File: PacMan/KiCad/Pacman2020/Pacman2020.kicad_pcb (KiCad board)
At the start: 2 copper layers, 109.2 x 73.7 mm, 50 parts, among them J1 DF22-1P-7.92DSA(05), J10 Conn_01x02, J11 Conn_01x02, J12 Conn_01x02, J13 Conn_01x08, J2 DF22-1P-7.92DSA(05), J3 DF22-1P-7.92DSA(05), J4 JST PH, J5 Conn_02x03_Odd_Even, J6 Conn_01x01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

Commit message: notes from design review 1
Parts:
- removed G***: LOGO, AERO_CUSTOM:pacman-logo-silkscreen
- removed J6, J7: Conn_01x01, Connector_Hirose:Hirose_DF63R-1P-3.96DSA_1x01_P3.96mm_Vertical
- moved R5 82.2 mm to (106.4, 140.8)
- moved J8 49.1 mm to (166.2, 144.5), turned to 270 degrees
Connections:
- J13 pad 4: +12V -> /CONTACTOR
- J13 pad 5: /PRECHARGE -> GND
- J13 pad 6: /CONTACTOR -> /SHUTDOWN_IN
- J13 pad 7: /SHUTDOWN_IN -> GND
- J13 pad 8: GND -> /PRECHARGE
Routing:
- net /SHUTDOWN_IN: track 18.2 -> 119.6 mm
- net /CONTACTOR: track 3.68 -> 58.3 mm
- net /PRECHARGE: track 2.07 -> 19.8 mm
- net GND: vias 7 -> 11

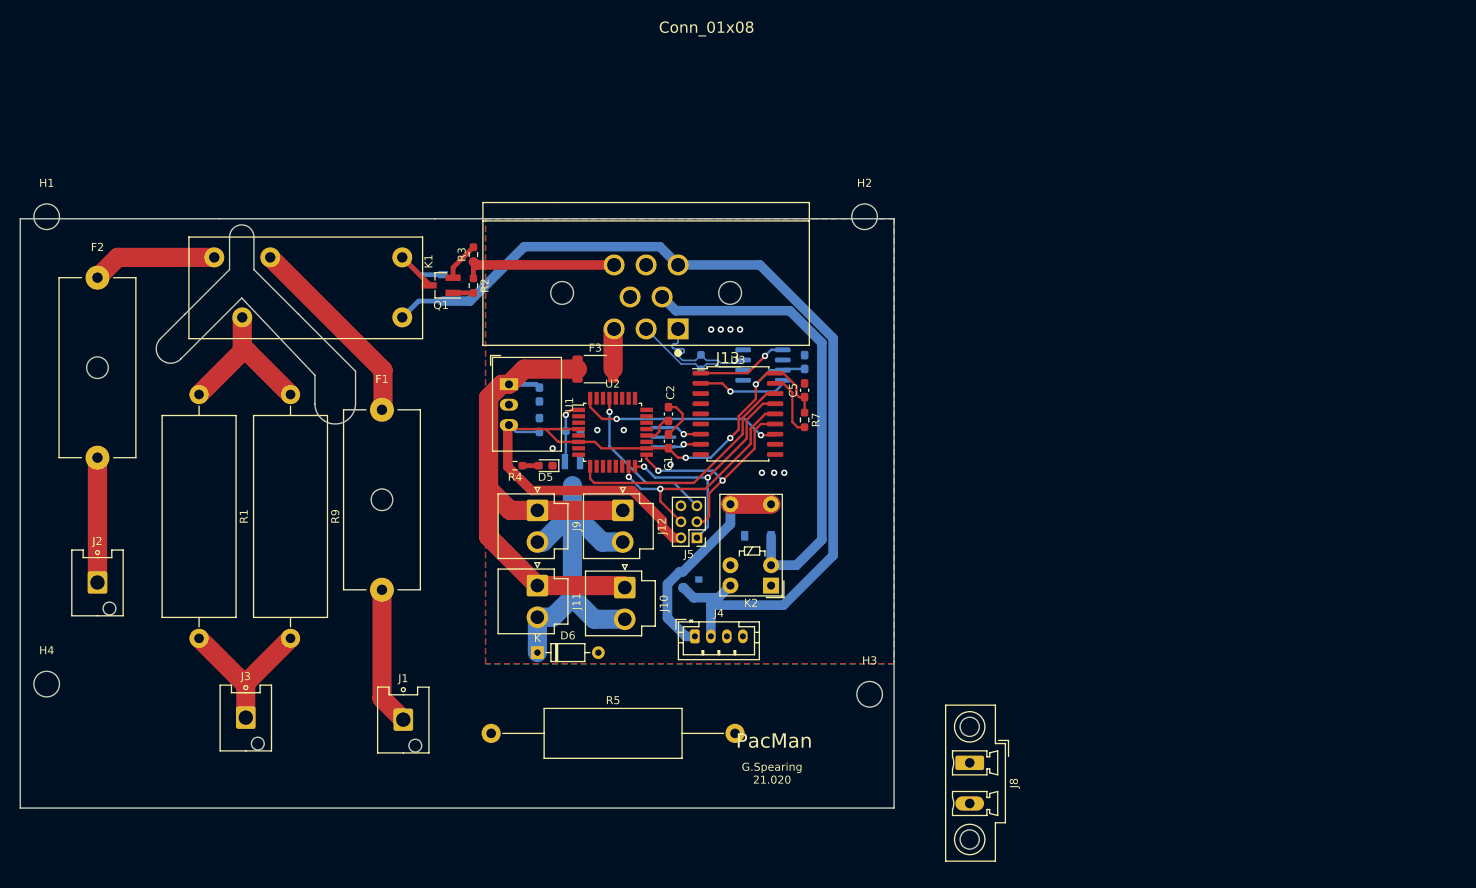
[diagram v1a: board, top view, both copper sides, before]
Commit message: remove ATMEGA, add BMS fan control
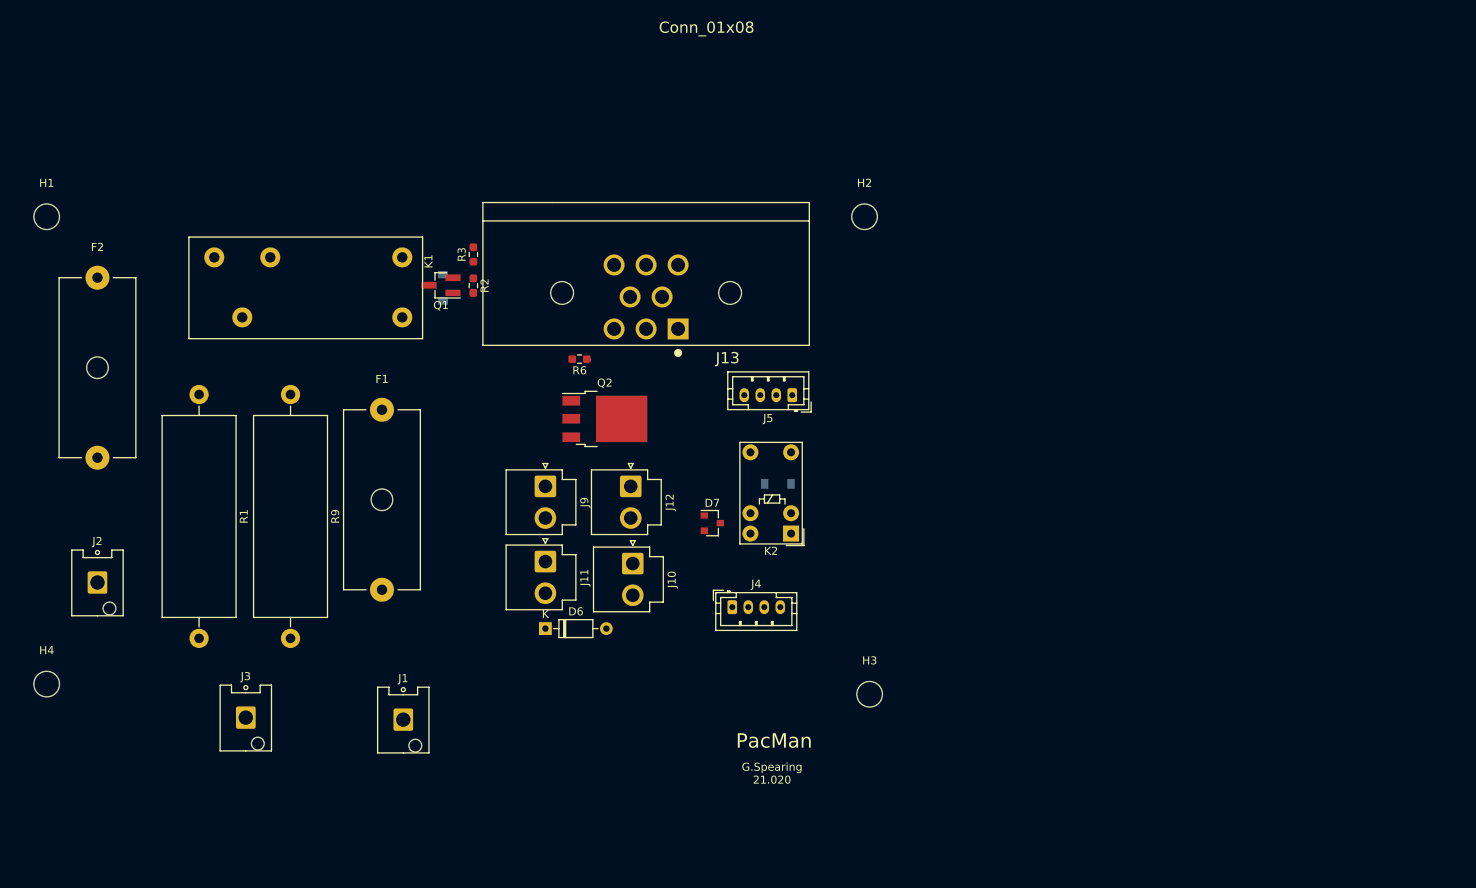
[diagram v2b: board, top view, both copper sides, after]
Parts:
- removed C1, C2, C5, C6: 0.1u, Capacitor_SMD:C_0603_1608Metric_Pad1.08x0.95mm_HandSolder
- removed C3: 1u, Capacitor_SMD:C_0603_1608Metric_Pad1.08x0.95mm_HandSolder
- removed C4: 10u, Capacitor_SMD:C_0603_1608Metric_Pad1.08x0.95mm_HandSolder
- removed D5: LED, LED_SMD:LED_0603_1608Metric_Pad1.05x0.95mm_HandSolder
- removed F3: MF-MSMF050, Fuse:Fuse_1812_4532Metric_Pad1.30x3.40mm_HandSolder
- removed J8: Conn_01x02, Connector_Phoenix_MC_HighVoltage:PhoenixContact_MCV_1,5_2-GF-5.08_1x02_P5.08mm_Vertical_ThreadedFlange_MountHole
- removed R4: 330, Resistor_SMD:R_0603_1608Metric_Pad0.98x0.95mm_HandSolder
- removed R5: 39k, Resistor_THT:R_Axial_DIN0617_L17.0mm_D6.0mm_P30.48mm_Horizontal
- removed R7: 10K, Resistor_SMD:R_0603_1608Metric_Pad0.98x0.95mm_HandSolder
- removed R8: 120, Resistor_SMD:R_0603_1608Metric_Pad0.98x0.95mm_HandSolder
- removed U1: R-785.0-1.0, Converter_DCDC:Converter_DCDC_RECOM_R-78E-0.5_THT
- removed U2: ATmega328P-AU, Package_QFP:TQFP-32_7x7mm_P0.8mm
- removed U3: MCP2515-xSO, Package_SO:SOIC-18W_7.5x11.6mm_P1.27mm
- removed U4: MCP2551-I-SN, Package_SO:SOIC-8_3.9x4.9mm_P1.27mm
- removed Y1: 16MHz, AERO_CUSTOM:Resonator_SMD_muRata_CSTxExxV-3Pin_3.0x1.1mm_HandSoldering
- D7, R6: moved to F.Cu
- J5: value Conn_02x03_Odd_Even -> Conn_01x04; footprint Connector_PinHeader_2.00mm:PinHeader_2x03_P2.00mm_Vertical -> Connector_JST:JST_PH_B4B-PH-K_1x04_P2.00mm_Vertical
- Q2: value DMN3404L -> Q_NMOS_GDS; footprint Package_TO_SOT_SMD:SOT-23_Handsoldering -> Package_TO_SOT_SMD:TO-252-3_TabPin2; moved to F.Cu
- moved J5 21.4 mm to (144.0, 98.5)
- moved R6 9.03 mm to (117.4, 94.0), turned to 180 degrees
- moved Q2 7.94 mm to (120.6, 101.5), turned to 0 degrees
- moved D7 7.53 mm to (134.0, 114.5)
- moved D2 6.96 mm to (142.2, 109.6)
- moved K2 6.96 mm to (143.9, 115.8)
- moved J4 5.93 mm to (136.5, 125.0)
- moved J10 3.16 mm to (124.1, 119.6)
- moved J11 3.16 mm to (113.1, 119.3)
- moved J12 3.16 mm to (123.8, 109.9)
- moved J9 3.16 mm to (113.1, 109.9)
- moved D6 3.16 mm to (113.1, 127.7)
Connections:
- net Net-(F1-Pad2) renamed /pre/discharge/INT-
- net Net-(F2-Pad2) renamed /pre/discharge/BATT+
- net Net-(J3-Pad1) renamed /pre/discharge/INT+
- D7 pad 1: /SHUTDOWN_IN -> /pre/discharge/AIR_B+
- D7 pad 2: /pre/discharge/AIR_B+ -> /SHUTDOWN_IN
- J13 pad 3: +12V -> /FAN_CTRL
- J13 pad 5: GND -> +12V
- J5 pad 1: /MISO -> /CAN+
- J5 pad 2: +5V -> /CAN-
- J5 pad 3: /SCK -> +12V
- J5 pad 4: /MOSI -> GND
- K2 pad 1: (no net) -> Net-(K2-Pad1)
- Q1 pad 2: Net-(Q1-Pad2) -> GND
- Q2 pad 2: GND -> /FAN_OUT
- Q2 pad 3: /FAN_OUT -> GND
- R3 pad 2: Net-(Q1-Pad2) -> GND
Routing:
- net /SHUTDOWN_IN: track 119.6 -> 0.00 mm
- net +5V: track 95.2 -> 0.00 mm, vias 3 -> 0
- net /12_IN: track 71.5 -> 0.00 mm
- net /CONTACTOR: track 58.3 -> 0.00 mm
- net /FAN_OUT: track 45.2 -> 0.00 mm
- net /MISO: track 31.4 -> 0.00 mm, vias 2 -> 0
- net /CAN_CS: track 30.7 -> 0.00 mm
- net /MOSI: track 30.4 -> 0.00 mm, vias 2 -> 0
- net /SCK: track 29.0 -> 0.00 mm, vias 2 -> 0
- net /pre/discharge/AIR_B+: track 27.2 -> 0.00 mm
- net /CAN_INT: track 25.7 -> 0.00 mm, vias 2 -> 0
- net Net-(F1-Pad1): track 24.9 -> 0.00 mm
- net /pre/discharge/INT+: track 20.4 -> 0.00 mm
- net Net-(K1-Pad5): track 20.1 -> 0.00 mm
- net /RESET: track 20.0 -> 0.00 mm, vias 1 -> 0
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- removed copper zone on B.Cu, net GND
- removed copper zone on F.Cu, net GND
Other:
- board outline removed

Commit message: update schematic and layout
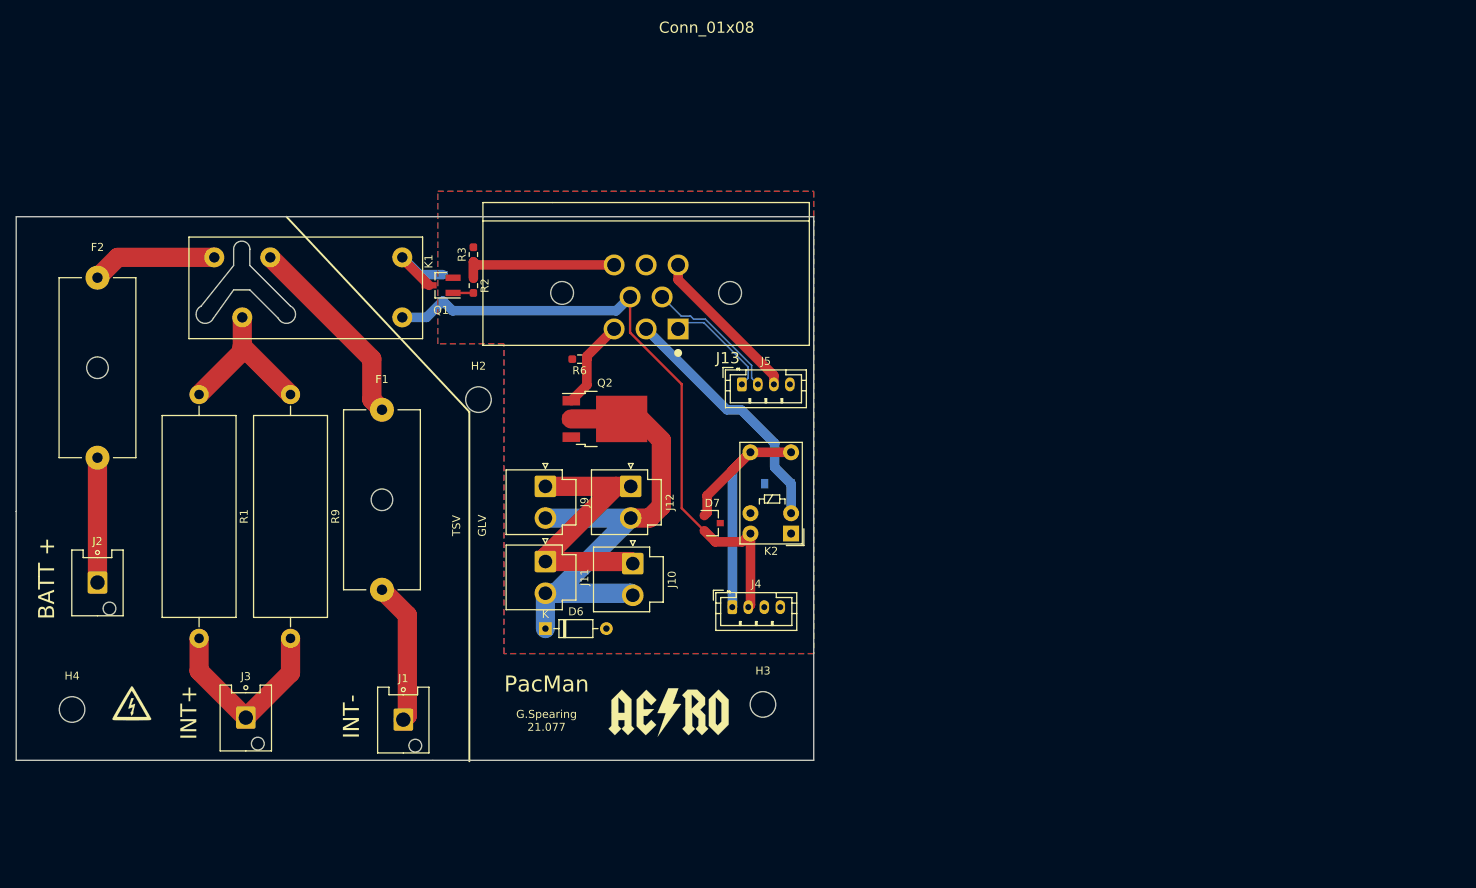
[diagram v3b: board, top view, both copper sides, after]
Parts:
- removed H1: MountingHole, MountingHole:MountingHole_3.2mm_M3
- added G***: LOGO, AERO_CUSTOM:AERO_Logo_15x6mm, F.Cu at (128.5, 138.2)
- added Ref**: Val**, AERO_Logo:hv_small, F.Cu at (61.5, 139.2)
- moved H2 53.4 mm to (104.8, 99.1)
- moved H3 13.4 mm to (140.3, 137.2)
- moved J5 6.44 mm to (137.7, 97.2), turned to 0 degrees
- moved H4 4.49 mm to (54.0, 137.8)
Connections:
- J13 pad 2: /CAN- -> /CONTACTOR
- J13 pad 4: /CONTACTOR -> /CAN-
- J13 pad 5: +12V -> /SHUTDOWN_IN
- J13 pad 6: /SHUTDOWN_IN -> +12V
- K2 pad 1: Net-(K2-Pad1) -> (no net)
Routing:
- net /SHUTDOWN_IN: track 0.00 -> 79.7 mm
- net /FAN_OUT: track 0.00 -> 65.7 mm
- net /pre/discharge/AIR_B+: track 0.00 -> 38.9 mm
- net /12_IN: track 0.00 -> 35.4 mm
- net /CONTACTOR: track 0.00 -> 31.6 mm
- net Net-(F1-Pad1): track 0.00 -> 24.8 mm
- net /pre/discharge/INT+: track 0.00 -> 24.5 mm
- net Net-(K1-Pad5): track 0.00 -> 20.4 mm
- net +12V: track 0.00 -> 19.9 mm
- net /PRECHARGE: track 0.00 -> 19.8 mm
- net /pre/discharge/INT-: track 0.00 -> 17.8 mm
- net /CAN-: track 0.00 -> 17.4 mm
- net Net-(F2-Pad1): track 0.00 -> 15.7 mm
- net /pre/discharge/BATT+: track 0.00 -> 15.6 mm
- net /CAN+: track 0.00 -> 13.9 mm
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- added copper zone on B.Cu, net GND
- added copper zone on F.Cu, net GND
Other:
- board outline added: 99.7 x 67.9 mm
- rule pad_to_mask_clearance: 0.05 -> 0
- board text added: "BATT +"
- board text added: "G.Spearing 21.077"
- board text added: "INT+"
- board text added: "INT-"
- board text added: "TSV GLV"
- board text removed: "G.Spearing 21.020"
